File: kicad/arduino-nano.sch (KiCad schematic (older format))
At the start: 27 parts, among them J4 USB_B, J5 AVR ISP, SW5 Reset, U4 CH340C, U5 ATmega328P-AU, Y1 16MHz

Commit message: kleinere Updates im Schaltplan
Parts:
- added C?: 10n, Capacitor_SMD:C_1206_3216Metric, symbol Device:C
- J4: symbol Connector:USB_B -> jbc-miniregler-rescue:USB_B-Connector
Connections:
- wire segments 136 -> 139
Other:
- note added: "TODO: notwendig?"
- moved on the sheet: SW5
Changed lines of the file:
@@
 	2250 4200 2600 4200
 $Comp
-L Connector:USB_B J4
+L jbc-miniregler-rescue:USB_B-Connector J4
 U 1 1 6095254E
 P 1550 6300
+AR Path="/6095254E" Ref="J4"  Part="1"
+AR Path="/608DBC3C/60930C19/6095254E" Ref="J4"  Part="1"
 F 0 "J4" H 1607 6767 50  0000 C CNN
 F 1 "USB_B" H 1607 6676 50  0000 C CNN
@@
 	4800 6100 5950 6100
 Wire Wire Line
-	5850 6000 5850 3950
-Wire Wire Line
 	5850 3950 5100 3950
 Wire Wire Line
@@
 L Switch:SW_Push SW?
 U 1 1 6099C47A
-P 6300 4350
+P 6300 4550
 AR Path="/608DBC3C/6099C47A" Ref="SW?"  Part="1"
 AR Path="/6099C47A" Ref="SW?"  Part="1"
 AR Path="/608DBC3C/60930C19/6099C47A" Ref="SW5"  Part="1"
-F 0 "SW5" V 6346 4302 50  0000 R CNN
-F 1 "Reset" V 6255 4302 50  0000 R CNN
-F 2 "htl_smd:SW_Push_5.1mm_H1.5mm" H 6300 4550 50  0001 C CNN
-F 3 "~" H 6300 4550 50  0001 C CNN
-F 4 "C318884" H 6300 4350 50  0001 C CNN "DistOrderNr"
-F 5 "LCSC" H 6300 4350 50  0001 C CNN "Distributor"
-F 6 "TS-1187A-B-A-B" H 6300 4350 50  0001 C CNN "ManPartNr"
-F 7 "XKB Connectivity" H 6300 4350 50  0001 C CNN "Manufacturer"
-F 8 "SPST 50mA @ 12VDC Vertical Round Button 160gf SMD Tactile Switches" H 6300 4350 50  0001 C CNN "Notes"
-F 9 "0.01" H 6300 4350 50  0001 C CNN "PriceEUR"
-F 10 "500" H 6300 4350 50  0001 C CNN "PriceForQty"
-F 11 "https://lcsc.com/product-detail/Tactile-Switches_XKB-Connectivity-TS-1187A-B-A-B_C318884.html" H 6300 4350 50  0001 C CNN "Weblink"
-	1    6300 4350
+F 0 "SW5" V 6346 4502 50  0000 R CNN
+F 1 "Reset" V 6255 4502 50  0000 R CNN
+F 2 "htl_smd:SW_Push_5.1mm_H1.5mm" H 6300 4750 50  0001 C CNN
+F 3 "~" H 6300 4750 50  0001 C CNN
+F 4 "C318884" H 6300 4550 50  0001 C CNN "DistOrderNr"
+F 5 "LCSC" H 6300 4550 50  0001 C CNN "Distributor"
+F 6 "TS-1187A-B-A-B" H 6300 4550 50  0001 C CNN "ManPartNr"
+F 7 "XKB Connectivity" H 6300 4550 50  0001 C CNN "Manufacturer"
+F 8 "SPST 50mA @ 12VDC Vertical Round Button 160gf SMD Tactile Switches" H 6300 4550 50  0001 C CNN "Notes"
+F 9 "0.01" H 6300 4550 50  0001 C CNN "PriceEUR"
+F 10 "500" H 6300 4550 50  0001 C CNN "PriceForQty"
+F 11 "https://lcsc.com/product-detail/Tactile-Switches_XKB-Connectivity-TS-1187A-B-A-B_C318884.html" H 6300 4550 50  0001 C CNN "Weblink"
+	1    6300 4550
 	0    -1   -1   0
 $EndComp
 Wire Wire Line
-	6300 4150 6300 3750
+	6300 4350 6300 4200
 $Comp
 L power:GND #PWR022
 U 1 1 609A896E
-P 6300 4550
-F 0 "#PWR022" H 6300 4300 50  0001 C CNN
-F 1 "GND" H 6305 4377 50  0000 C CNN
-F 2 "" H 6300 4550 50  0001 C CNN
-F 3 "" H 6300 4550 50  0001 C CNN
-	1    6300 4550
+P 6300 4750
+F 0 "#PWR022" H 6300 4500 50  0001 C CNN
+F 1 "GND" H 6305 4577 50  0000 C CNN
+F 2 "" H 6300 4750 50  0001 C CNN
+F 3 "" H 6300 4750 50  0001 C CNN
+	1    6300 4750
 	1    0    0    -1
 $EndComp
@@
 Wire Wire Line
 	1850 6100 2250 6100
+Wire Wire Line
+	5850 6000 5850 3950
+Wire Wire Line
+	6300 4200 6700 4200
+Wire Wire Line
+	6700 4200 6700 4450
+Connection ~ 6300 4200
+Wire Wire Line
+	6300 4200 6300 3750
+$Comp
+L power:GND #PWR?
+U 1 1 6097814E
+P 6700 4750
+F 0 "#PWR?" H 6700 4500 50  0001 C CNN
+F 1 "GND" H 6705 4577 50  0000 C CNN
+F 2 "" H 6700 4750 50  0001 C CNN
+F 3 "" H 6700 4750 50  0001 C CNN
+	1    6700 4750
+	1    0    0    -1
+$EndComp
+Text Notes 6450 5050 0    50   ~ 0
+TODO: notwendig?
+$Comp
+L Device:C C?
+U 1 1 6097B642
+P 6700 4600
+F 0 "C?" H 6815 4646 50  0000 L CNN
+F 1 "10n" H 6815 4555 50  0000 L CNN
+F 2 "Capacitor_SMD:C_1206_3216Metric" H 6738 4450 50  0001 C CNN
+F 3 "~" H 6700 4600 50  0001 C CNN
+F 4 "C525316" H 6700 4600 50  0001 C CNN "DistOrderNr"
+F 5 "LCSC" H 6700 4600 50  0001 C CNN "Distributor"
+F 6 "FN31X103K500PXG" H 6700 4600 50  0001 C CNN "ManPartNr"
+F 7 "PSA(Prosperity Dielectrics)" H 6700 4600 50  0001 C CNN "Manufacturer"
+F 8 "10nF ±10% 50V X7R  Multilayer Ceramic Capacitors MLCC" H 6700 4600 50  0001 C CNN "Notes"
+F 9 "0.0106" H 6700 4600 50  0001 C CNN "PriceEUR"
+F 10 "500" H 6700 4600 50  0001 C CNN "PriceForQty"
+	1    6700 4600
+	1    0    0    -1
+$EndComp
 $EndSCHEMATC

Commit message: Reviews und ein paar Verbesserungen
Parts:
- J4: footprint Connector_USB:USB_B_Lumberg_2411_02_Horizontal -> htl_connectors:USB_B_Lumberg_2411_02_Horizontal
- gave numbers to parts that had none: 1
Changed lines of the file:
@@
 F 1 "CH340C" H 3950 5850 50  0000 C CNN
 F 2 "Package_SO:SOIC-16_3.9x9.9mm_P1.27mm" H 3800 5850 50  0001 L CNN
-F 3 "http://www.datasheet5.com/pdf-local-2195953" H 3400 7200 50  0001 C CNN
+F 3 "https://www.mpja.com/download/35227cpdata.pdf" H 3400 7200 50  0001 C CNN
 F 4 "WCH(Jiangsu Qin Heng)" H 3750 6400 50  0001 C CNN "Manufacturer"
 F 5 "LCSC" H 3750 6400 50  0001 C CNN "Distributor"
@@
 F 0 "J4" H 1607 6767 50  0000 C CNN
 F 1 "USB_B" H 1607 6676 50  0000 C CNN
-F 2 "Connector_USB:USB_B_Lumberg_2411_02_Horizontal" H 1700 6250 50  0001 C CNN
+F 2 "htl_connectors:USB_B_Lumberg_2411_02_Horizontal" H 1700 6250 50  0001 C CNN
 F 3 " ~" H 1700 6250 50  0001 C CNN
 F 4 "C46392" H 1550 6300 50  0001 C CNN "DistOrderNr"
@@
 	6300 4200 6300 3750
 $Comp
-L power:GND #PWR?
+L power:GND #PWR065
 U 1 1 6097814E
 P 6700 4750
-F 0 "#PWR?" H 6700 4500 50  0001 C CNN
+F 0 "#PWR065" H 6700 4500 50  0001 C CNN
 F 1 "GND" H 6705 4577 50  0000 C CNN
 F 2 "" H 6700 4750 50  0001 C CNN
@@
 TODO: notwendig?
 $Comp
-L Device:C C?
+L Device:C C38
 U 1 1 6097B642
 P 6700 4600
-F 0 "C?" H 6815 4646 50  0000 L CNN
+F 0 "C38" H 6815 4646 50  0000 L CNN
 F 1 "10n" H 6815 4555 50  0000 L CNN
 F 2 "Capacitor_SMD:C_1206_3216Metric" H 6738 4450 50  0001 C CNN

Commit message: WIP Layout, TODO: DRC
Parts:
- D4: footprint Diode_SMD:D_SMA -> htl_smd:D_SMA_wide
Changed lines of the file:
@@
 F 0 "D4" V 2204 4628 50  0000 L CNN
 F 1 "SS210" V 2295 4628 50  0000 L CNN
-F 2 "Diode_SMD:D_SMA" H 2250 4550 50  0001 C CNN
+F 2 "htl_smd:D_SMA_wide" H 2250 4550 50  0001 C CNN
 F 3 "~" H 2250 4550 50  0001 C CNN
 F 4 "C2683692" H 2250 4550 50  0001 C CNN "DistOrderNr"

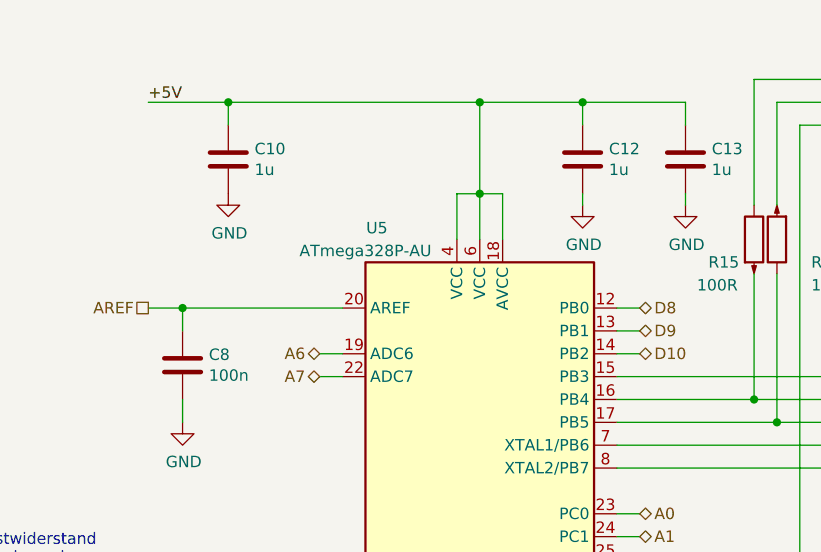
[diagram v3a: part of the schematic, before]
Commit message: OPV-Polaritätsoption, Zusatzfilter und Strombegrenzung
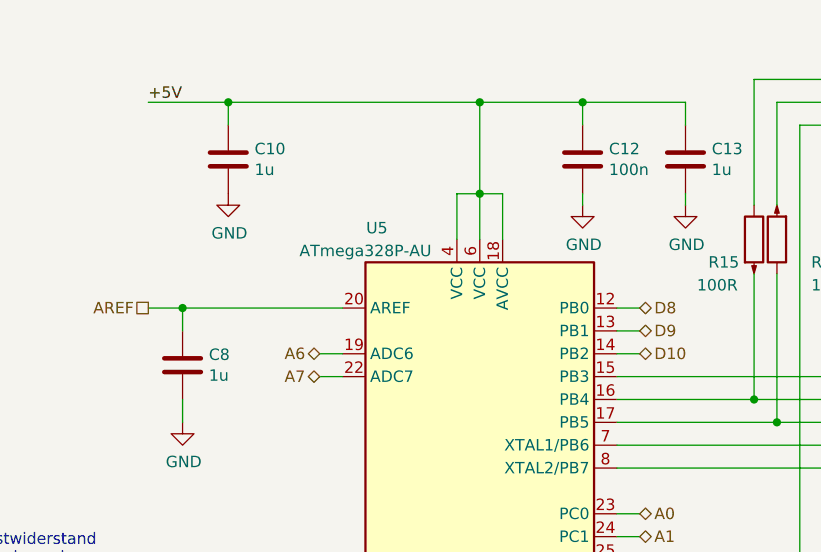
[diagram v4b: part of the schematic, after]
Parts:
- renumbered C8 to C12, C12 to C8
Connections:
- net +5V: now also C12.2; no longer C8.1
- net AREF: now also C8.1; no longer C12.2
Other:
- moved on the sheet: C12, C8
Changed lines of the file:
@@
 L Device:C C?
 U 1 1 609A9798
-P 3200 2500
+P 4950 1600
 AR Path="/5F64F622/609A9798" Ref="C?"  Part="1"
 AR Path="/5F78AFC8/609A9798" Ref="C?"  Part="1"
@@
 AR Path="/5F8D661A/609A9798" Ref="C?"  Part="1"
 AR Path="/608DBC3C/60930C19/60930D3D/609A9798" Ref="C?"  Part="1"
-AR Path="/608DBC3C/60930C19/609A9798" Ref="C8"  Part="1"
-F 0 "C8" H 3085 2454 50  0000 R CNN
-F 1 "100n" H 3085 2545 50  0000 R CNN
-F 2 "Capacitor_SMD:C_1206_3216Metric" H 3238 2350 50  0001 C CNN
-F 3 "https://datasheet.lcsc.com/szlcsc/1811151136_Walsin-Tech-Corp-0603B104K160CT_C80516.pdf" H 3200 2500 50  0001 C CNN
-F 4 "LCSC" H 3200 2500 50  0001 C CNN "Distributor"
-F 5 "PSA(Prosperity Dielectrics)" H 3200 2500 50  0001 C CNN "Manufacturer"
-F 6 "100nF ±10% 50V X7R Multilayer Ceramic Capacitors MLCC" H 3200 2500 50  0001 C CNN "Notes"
-F 7 "" H 3200 2500 50  0001 C CNN "OrderNr"
-F 8 "" H 3200 2500 50  0001 C CNN "PartNr"
-F 9 "0.0093" H 3200 2500 50  0001 C CNN "PriceEUR"
-F 10 "500" H 3200 2500 50  0001 C CNN "PriceForQty"
-F 11 "https://lcsc.com/product-detail/Multilayer-Ceramic-Capacitors-MLCC-SMD-SMT_Walsin-Tech-Corp-0603B104K160CT_C80516.html" H 3200 2500 50  0001 C CNN "Weblink"
-F 12 "C464972" H 3200 2500 50  0001 C CNN "DistOrderNr"
-F 13 "FN31X104K500PXG" H 3200 2500 50  0001 C CNN "ManPartNr"
-	1    3200 2500
+AR Path="/608DBC3C/60930C19/609A9798" Ref="C12"  Part="1"
+F 0 "C12" H 4835 1554 50  0000 R CNN
+F 1 "100n" H 4835 1645 50  0000 R CNN
+F 2 "Capacitor_SMD:C_1206_3216Metric" H 4988 1450 50  0001 C CNN
+F 3 "https://datasheet.lcsc.com/szlcsc/1811151136_Walsin-Tech-Corp-0603B104K160CT_C80516.pdf" H 4950 1600 50  0001 C CNN
+F 4 "LCSC" H 4950 1600 50  0001 C CNN "Distributor"
+F 5 "PSA(Prosperity Dielectrics)" H 4950 1600 50  0001 C CNN "Manufacturer"
+F 6 "100nF ±10% 50V X7R Multilayer Ceramic Capacitors MLCC" H 4950 1600 50  0001 C CNN "Notes"
+F 7 "" H 4950 1600 50  0001 C CNN "OrderNr"
+F 8 "" H 4950 1600 50  0001 C CNN "PartNr"
+F 9 "0.0093" H 4950 1600 50  0001 C CNN "PriceEUR"
+F 10 "500" H 4950 1600 50  0001 C CNN "PriceForQty"
+F 11 "https://lcsc.com/product-detail/Multilayer-Ceramic-Capacitors-MLCC-SMD-SMT_Walsin-Tech-Corp-0603B104K160CT_C80516.html" H 4950 1600 50  0001 C CNN "Weblink"
+F 12 "C464972" H 4950 1600 50  0001 C CNN "DistOrderNr"
+F 13 "FN31X104K500PXG" H 4950 1600 50  0001 C CNN "ManPartNr"
+	1    4950 1600
 	-1   0    0    1
 $EndComp
@@
 L Device:C C?
 U 1 1 609FC0C3
-P 4950 1600
+P 3200 2500
 AR Path="/608DBC6E/609FC0C3" Ref="C?"  Part="1"
-AR Path="/608DBC3C/60930C19/609FC0C3" Ref="C12"  Part="1"
-F 0 "C12" H 5065 1646 50  0000 L CNN
-F 1 "1u" H 5065 1555 50  0000 L CNN
-F 2 "Capacitor_SMD:C_1206_3216Metric" H 4988 1450 50  0001 C CNN
-F 3 "~" H 4950 1600 50  0001 C CNN
-F 4 "C1848" H 4950 1600 50  0001 C CNN "DistOrderNr"
-F 5 "LCSC" H 4950 1600 50  0001 C CNN "Distributor"
-F 6 "CL31B105KBHNNNE" H 4950 1600 50  0001 C CNN "ManPartNr"
-F 7 "Samsung" H 4950 1600 50  0001 C CNN "Manufacturer"
-F 8 "1uF ±10% 50V X7R Multilayer Ceramic Capacitors MLCC" H 4950 1600 50  0001 C CNN "Notes"
-F 9 "0.0225" H 4950 1600 50  0001 C CNN "PriceEUR"
-F 10 "100" H 4950 1600 50  0001 C CNN "PriceForQty"
-	1    4950 1600
-	1    0    0    -1
-$EndComp
+AR Path="/608DBC3C/60930C19/609FC0C3" Ref="C8"  Part="1"
+F 0 "C8" H 3315 2546 50  0000 L CNN
+F 1 "1u" H 3315 2455 50  0000 L CNN
+F 2 "Capacitor_SMD:C_1206_3216Metric" H 3238 2350 50  0001 C CNN
+F 3 "~" H 3200 2500 50  0001 C CNN
+F 4 "C1848" H 3200 2500 50  0001 C CNN "DistOrderNr"
+F 5 "LCSC" H 3200 2500 50  0001 C CNN "Distributor"
+F 6 "CL31B105KBHNNNE" H 3200 2500 50  0001 C CNN "ManPartNr"
+F 7 "Samsung" H 3200 2500 50  0001 C CNN "Manufacturer"
+F 8 "1uF ±10% 50V X7R Multilayer Ceramic Capacitors MLCC" H 3200 2500 50  0001 C CNN "Notes"
+F 9 "0.0225" H 3200 2500 50  0001 C CNN "PriceEUR"
+F 10 "100" H 3200 2500 50  0001 C CNN "PriceForQty"
+	1    3200 2500
+	1    0    0    -1
+$EndComp
